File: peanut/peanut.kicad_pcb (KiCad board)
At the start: 4 copper layers, 51 x 24.5 mm, 70 parts, among them J1 USB-C, J2 PYRO_OUT, J3 Battery JST, J4 Arming, Q1 NMOS, Q2 NMOS, Q3 NMOS, Q4 NMOS, Q5 PMOS, U1 MS5611-01BA, U3 ESP32-C3FH4, U4 LM3671MF, U5 TPS2116DRL, Y1 40MHz

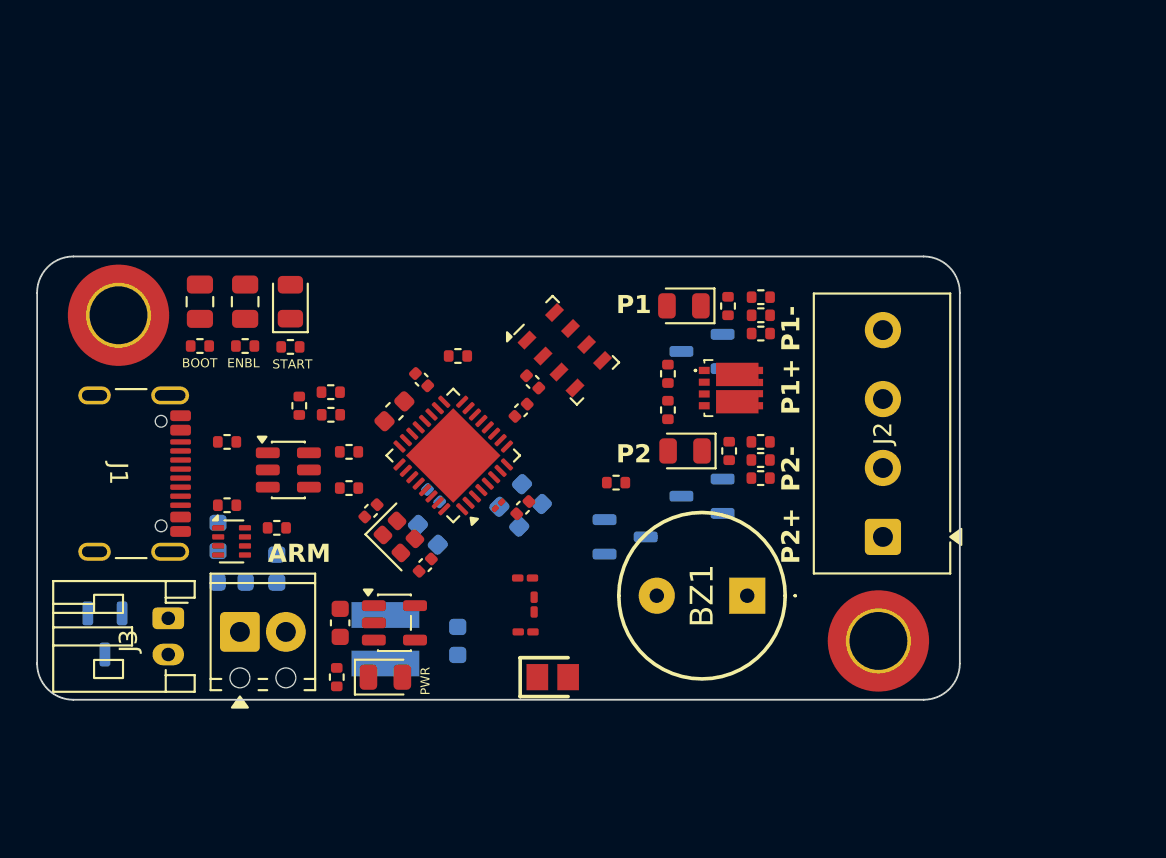
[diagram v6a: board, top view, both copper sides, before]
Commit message: feat: Added inner layer pours
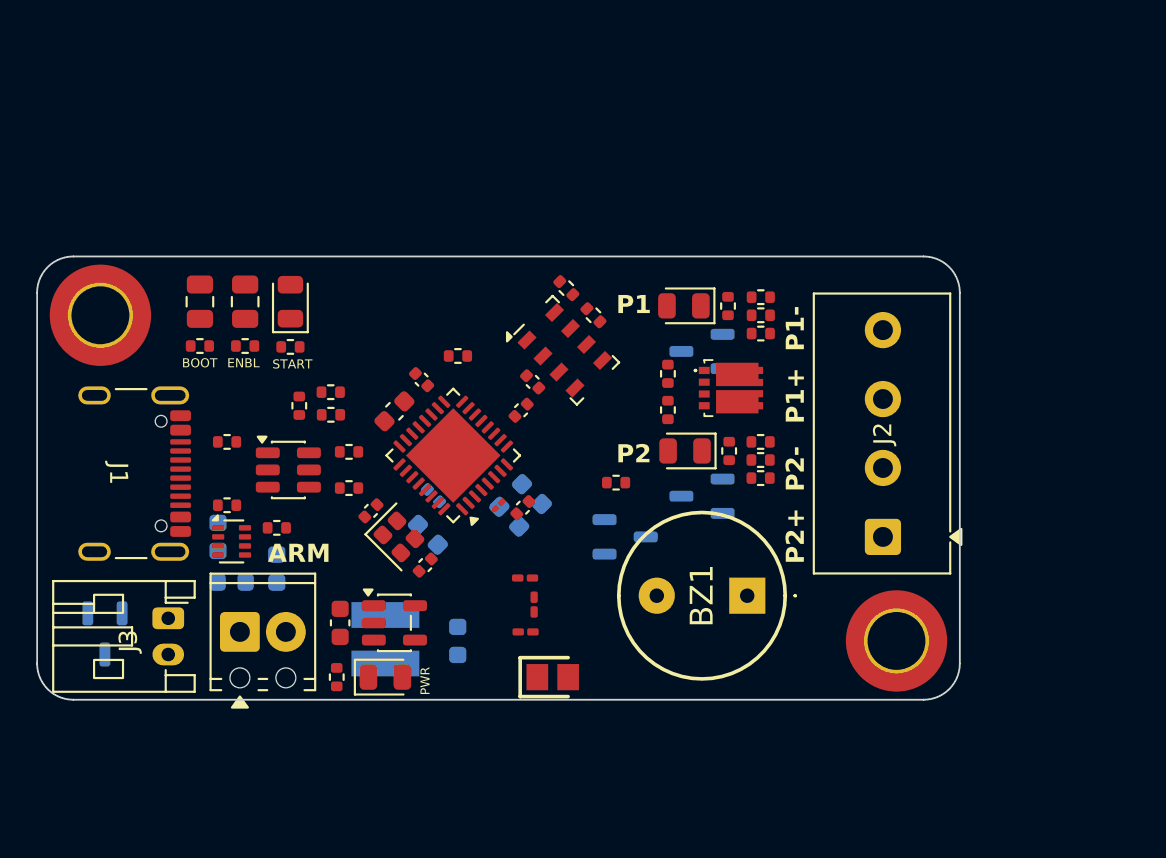
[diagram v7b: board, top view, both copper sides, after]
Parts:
- added R25: 2k2, Resistor_SMD:R_0402_1005Metric, F.Cu at (125.8, 91.8)
- added R26: 2k2, Resistor_SMD:R_0402_1005Metric, F.Cu at (124.2, 90.2)
- moved H1 1.00 mm to (98.5, 91.8)
- moved H2 1.00 mm to (142.5, 109.8)
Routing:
- added copper zone on In2.Cu, net 3V3
- added copper zone on In1.Cu, net GND

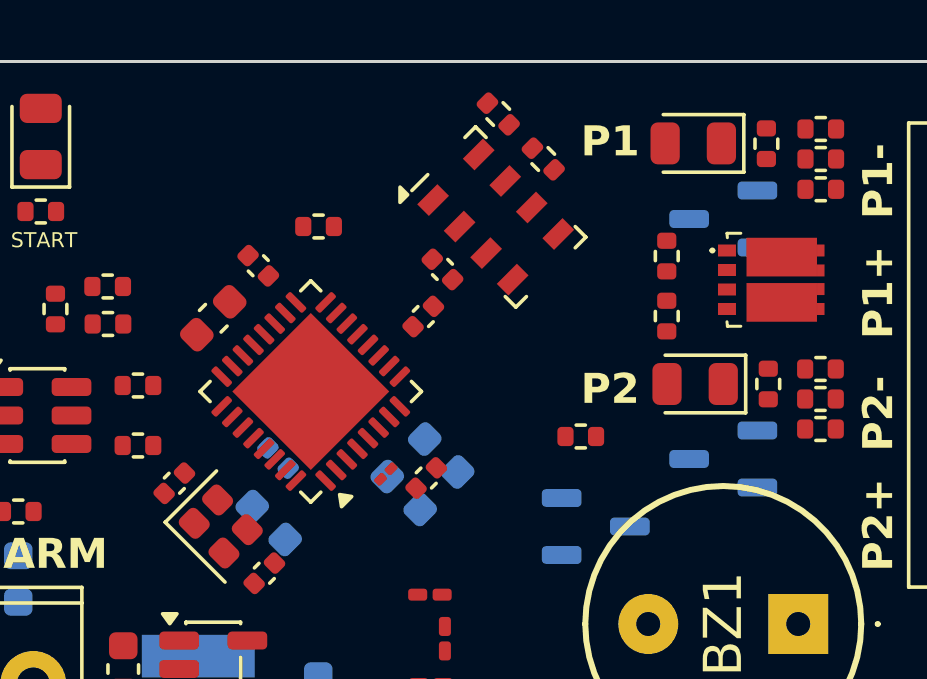
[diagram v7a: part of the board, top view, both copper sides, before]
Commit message: feat: 100n capacitors to 0603
Since there is sufficient space, the 100n capacitors have been increased
to 0603 size and all placed on the back of the board. This allows the
board to be squished in further slightly.
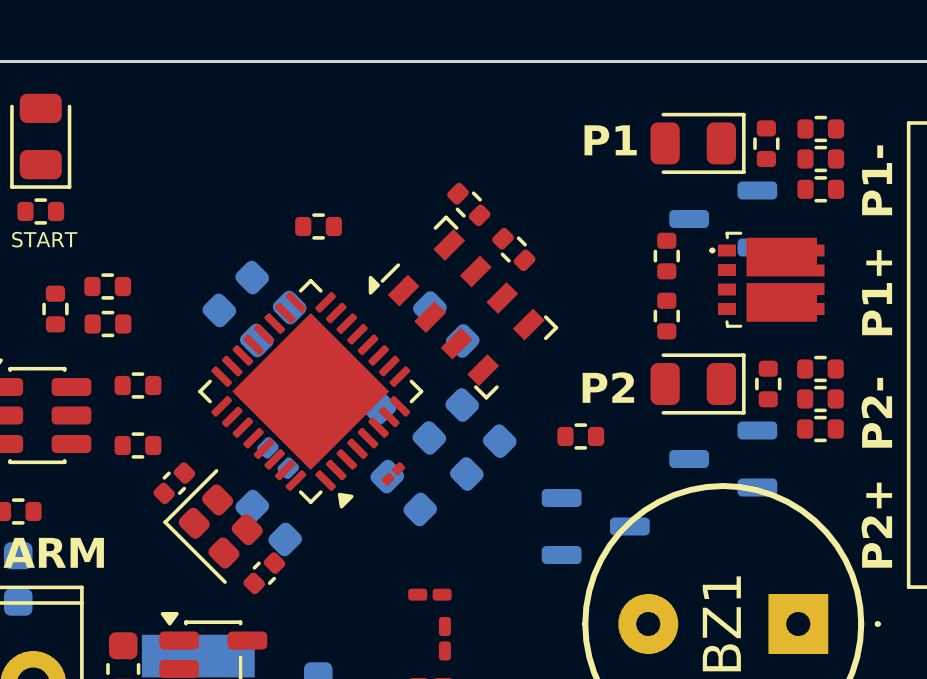
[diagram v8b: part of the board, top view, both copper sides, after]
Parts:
- C10: moved to B.Cu
- C11, C3, C5, C9: footprint Capacitor_SMD:C_0402_1005Metric -> Capacitor_SMD:C_0603_1608Metric; moved to B.Cu
- moved C9 3.20 mm to (119.8, 99.5), turned to -45 degrees
- moved R25 3.17 mm to (124.8, 94.8)
- moved R26 3.17 mm to (123.3, 93.3)
- moved U1 3.17 mm to (123.2, 96.7)
- moved C11 2.01 mm to (116.8, 97.2), turned to -135 degrees
- moved C5 1.99 mm to (122.5, 100.5)
- moved C3 1.84 mm to (122.5, 97.3)
- moved C4 1.40 mm to (123.8, 101.7), turned to 45 degrees
- moved C10 1.10 mm to (115.5, 96.2)
- moved L1 0.25 mm to (120.8, 102.2)
- moved D3 0.06 mm to (130.8, 99.2)
